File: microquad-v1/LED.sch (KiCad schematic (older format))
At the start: 2 parts

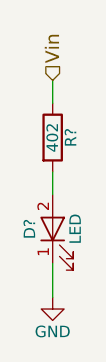
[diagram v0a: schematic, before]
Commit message: Fixed DRC errors (the ladybug is now happy)
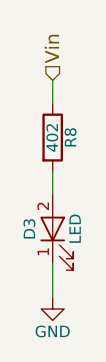
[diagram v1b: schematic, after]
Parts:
- gave numbers to parts that had none: 2
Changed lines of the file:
@@
 $Descr A4 11693 8268
 encoding utf-8
-Sheet 7 8
+Sheet 7 9
 Title ""
 Date ""
@@
 $EndDescr
 $Comp
-L LED D?
+L LED D2
 U 1 1 59F67341
 P 4850 3100
-F 0 "D?" H 4850 3200 50  0000 C CNN
+AR Path="/59F6B2DC/59F67341" Ref="D2"  Part="1"
+AR Path="/59F6B438/59F67341" Ref="D3"  Part="1"
+F 0 "D3" H 4850 3200 50  0000 C CNN
 F 1 "LED" H 4850 3000 50  0000 C CNN
 F 2 "" H 4850 3100 50  0001 C CNN
@@
 $EndComp
 $Comp
-L GND #PWR?
+L GND #PWR039
 U 1 1 59F673C8
 P 4850 3400
-F 0 "#PWR?" H 4850 3150 50  0001 C CNN
+AR Path="/59F6B2DC/59F673C8" Ref="#PWR039"  Part="1"
+AR Path="/59F6B438/59F673C8" Ref="#PWR040"  Part="1"
+F 0 "#PWR040" H 4850 3150 50  0001 C CNN
 F 1 "GND" H 4850 3250 50  0000 C CNN
 F 2 "" H 4850 3400 50  0001 C CNN
@@
 $EndComp
 $Comp
-L R R?
+L R R7
 U 1 1 59F67414
 P 4850 2700
-F 0 "R?" V 4930 2700 50  0000 C CNN
+AR Path="/59F6B2DC/59F67414" Ref="R7"  Part="1"
+AR Path="/59F6B438/59F67414" Ref="R8"  Part="1"
+F 0 "R8" V 4930 2700 50  0000 C CNN
 F 1 "402" V 4850 2700 50  0000 C CNN
 F 2 "" V 4780 2700 50  0001 C CNN

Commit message: Added layout for transistor
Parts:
- D2: footprint (none) -> LEDs:LED_0805
- R7: footprint (none) -> Resistors_SMD:R_0603
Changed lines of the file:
@@
 F 0 "D3" H 4850 3200 50  0000 C CNN
 F 1 "LED" H 4850 3000 50  0000 C CNN
-F 2 "" H 4850 3100 50  0001 C CNN
+F 2 "LEDs:LED_0805" H 4850 3100 50  0001 C CNN
 F 3 "" H 4850 3100 50  0001 C CNN
 	1    4850 3100
@@
 $EndComp
 $Comp
-L GND #PWR31
+L GND #PWR033
 U 1 1 59F673C8
 P 4850 3400
-AR Path="/59F6B2DC/59F673C8" Ref="#PWR31"  Part="1"
-AR Path="/59F6B438/59F673C8" Ref="#PWR32"  Part="1"
-F 0 "#PWR32" H 4850 3150 50  0001 C CNN
+AR Path="/59F6B2DC/59F673C8" Ref="#PWR033"  Part="1"
+AR Path="/59F6B438/59F673C8" Ref="#PWR034"  Part="1"
+F 0 "#PWR034" H 4850 3150 50  0001 C CNN
 F 1 "GND" H 4850 3250 50  0000 C CNN
 F 2 "" H 4850 3400 50  0001 C CNN
@@
 F 0 "R8" V 4930 2700 50  0000 C CNN
 F 1 "402" V 4850 2700 50  0000 C CNN
-F 2 "" V 4780 2700 50  0001 C CNN
+F 2 "Resistors_SMD:R_0603" V 4780 2700 50  0001 C CNN
 F 3 "" H 4850 2700 50  0001 C CNN
 	1    4850 2700

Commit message: Finished in-class work 10/2
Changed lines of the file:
@@
 $Descr A4 11693 8268
 encoding utf-8
-Sheet 7 15
+Sheet 6 15
 Title ""
 Date ""
@@
 AR Path="/59F6B2DC/59F67341" Ref="D2"  Part="1"
 AR Path="/59F6B438/59F67341" Ref="D3"  Part="1"
-F 0 "D3" H 4850 3200 50  0000 C CNN
+F 0 "D2" H 4850 3200 50  0000 C CNN
 F 1 "LED" H 4850 3000 50  0000 C CNN
 F 2 "LEDs:LED_0805" H 4850 3100 50  0001 C CNN
@@
 AR Path="/59F6B2DC/59F673C8" Ref="#PWR033"  Part="1"
 AR Path="/59F6B438/59F673C8" Ref="#PWR034"  Part="1"
-F 0 "#PWR034" H 4850 3150 50  0001 C CNN
+F 0 "#PWR033" H 4850 3150 50  0001 C CNN
 F 1 "GND" H 4850 3250 50  0000 C CNN
 F 2 "" H 4850 3400 50  0001 C CNN
@@
 AR Path="/59F6B2DC/59F67414" Ref="R7"  Part="1"
 AR Path="/59F6B438/59F67414" Ref="R8"  Part="1"
-F 0 "R8" V 4930 2700 50  0000 C CNN
+F 0 "R7" V 4930 2700 50  0000 C CNN
 F 1 "402" V 4850 2700 50  0000 C CNN
 F 2 "Resistors_SMD:R_0603" V 4780 2700 50  0001 C CNN

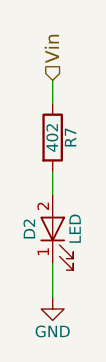
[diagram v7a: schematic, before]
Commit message: Initial power routing to all major chips
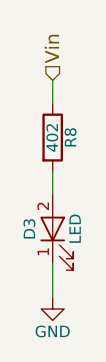
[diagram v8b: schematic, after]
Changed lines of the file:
@@
 AR Path="/59F6B2DC/59F67341" Ref="D2"  Part="1"
 AR Path="/59F6B438/59F67341" Ref="D3"  Part="1"
-F 0 "D2" H 4850 3200 50  0000 C CNN
+F 0 "D3" H 4850 3200 50  0000 C CNN
 F 1 "LED" H 4850 3000 50  0000 C CNN
 F 2 "LEDs:LED_0805" H 4850 3100 50  0001 C CNN
@@
 AR Path="/59F6B2DC/59F67414" Ref="R7"  Part="1"
 AR Path="/59F6B438/59F67414" Ref="R8"  Part="1"
-F 0 "R7" V 4930 2700 50  0000 C CNN
+F 0 "R8" V 4930 2700 50  0000 C CNN
 F 1 "402" V 4850 2700 50  0000 C CNN
 F 2 "Resistors_SMD:R_0603" V 4780 2700 50  0001 C CNN
